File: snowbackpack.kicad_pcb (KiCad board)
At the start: 2 copper layers, 39.6 x 18 mm, 86 parts, among them J10 Conn_01x01_Pin, J11 Conn_01x01_Pin, J12 Conn_01x01_Pin, J13 Conn_01x01_Pin, J2 Conn_01x01_Pin, J3 Conn_01x01_Pin, J4 Conn_01x01_Pin, J5 Conn_01x01_Pin, J6 Conn_01x01_Pin, J7 Conn_01x01_Pin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

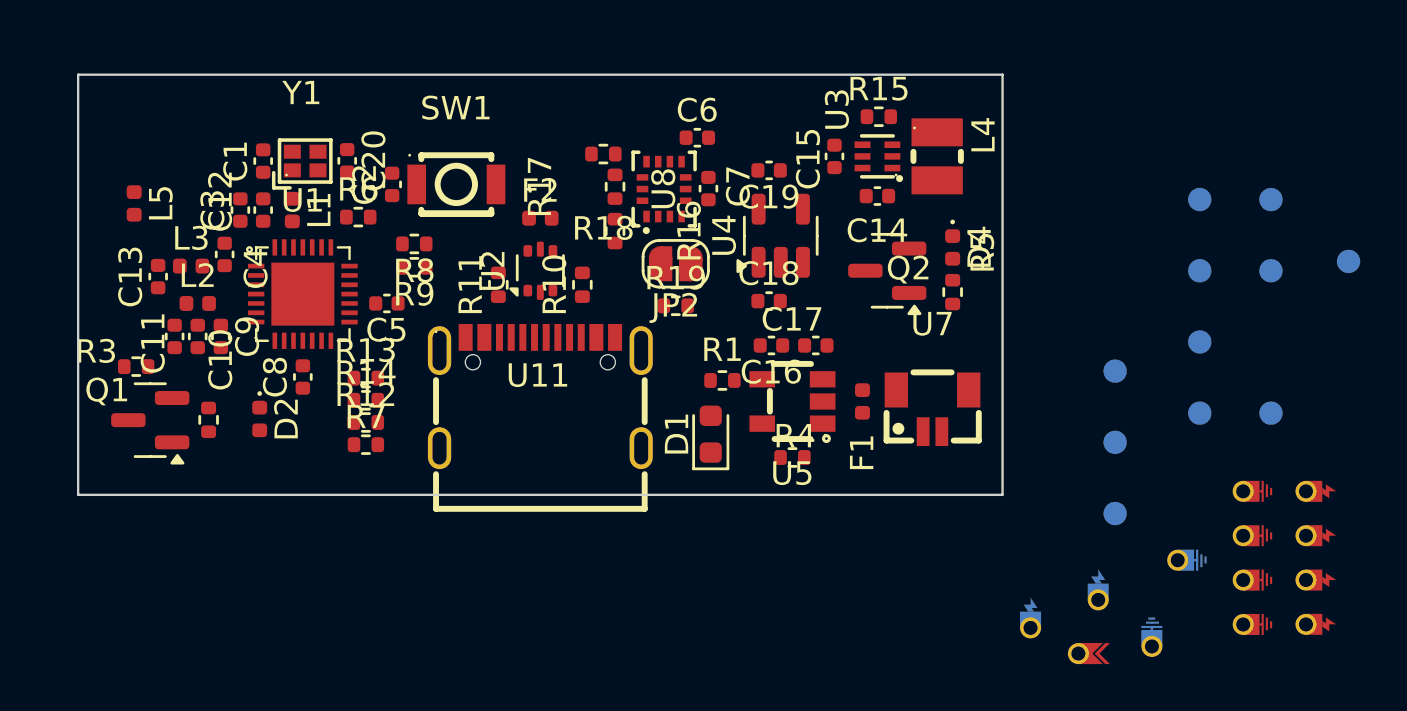
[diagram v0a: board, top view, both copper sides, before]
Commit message: First pcb routing
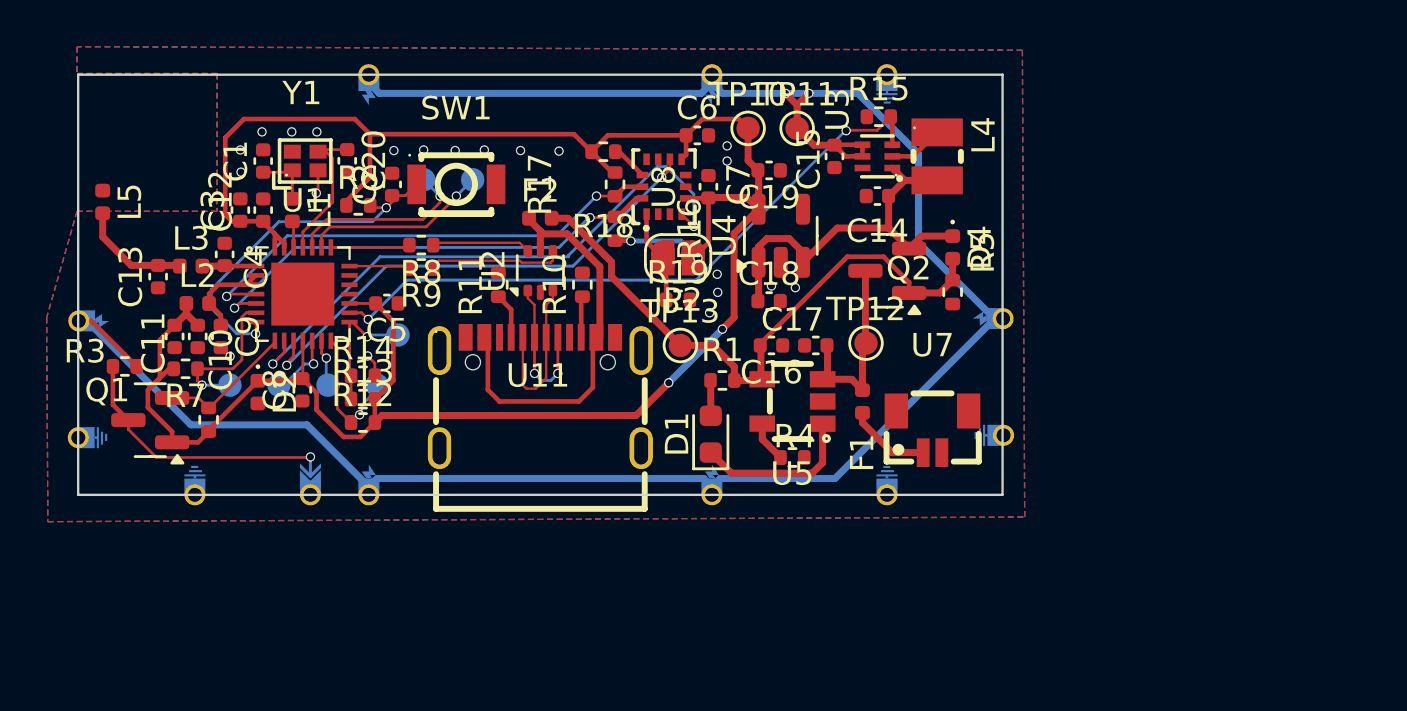
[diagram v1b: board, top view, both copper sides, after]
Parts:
- removed J12: Conn_01x01_Pin, Custom:matrix-pad-gn
- J10, J11, J13, J6, J7, J8, J9, JP1: moved to B.Cu
- TP10, TP11, TP12, TP13: moved to F.Cu
- moved J2 46.1 mm to (74.6, 97.5), turned to 0 degrees
- moved J8 45.8 mm to (86.5, 82.6), turned to -90 degrees
- moved J3 44.5 mm to (74.6, 92.5), turned to 0 degrees
- moved TP5 43.2 mm to (82.6, 95.3)
- moved J4 42.9 mm to (79.0, 99.4), turned to 90 degrees
- moved TP6 40.7 mm to (84.7, 95.3)
- moved TP14 37.9 mm to (80.5, 95.3)
- moved TP9 37.7 mm to (90.9, 86.5)
- moved TP8 37.7 mm to (88.8, 86.5)
- moved JP1 34.4 mm to (83.9, 99.4), turned to 90 degrees
- moved J7 32.3 mm to (101.2, 82.6), turned to -90 degrees
- moved TP15 31.7 mm to (86.8, 95.3)
- moved TP16 31.7 mm to (87.7, 93.2)
- moved J5 28.9 mm to (86.4, 99.4)
- moved J9 26.8 mm to (101.1, 99.4), turned to 90 degrees
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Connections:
- JP1 pad 1: Net-(JP1-A) -> unconnected-(JP1-A-Pad1)
- JP1 pad 2: unconnected-(JP1-B-Pad2) -> Net-(JP1-B)
- Q1 pad 3: Net-(JP1-A) -> Net-(JP1-B)
- R3 pad 2: Net-(JP1-A) -> Net-(JP1-B)
- U1 pad 4: SDA -> SCL
- U1 pad 5: SCL -> SDA
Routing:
- net VDD33: track 0.02 -> 103.3 mm, vias 0 -> 4
- net VDD5: track 0.00 -> 89.1 mm, vias 0 -> 2
- net 5VEN: track 0.00 -> 28.1 mm, vias 0 -> 2
- net VCCUSB: track 0.00 -> 26.0 mm
- net INT1: track 0.00 -> 25.4 mm, vias 0 -> 2
- net INT2: track 0.00 -> 21.5 mm, vias 0 -> 2
- net SCL: track 0.00 -> 21.1 mm, vias 0 -> 2
- net SDA: track 0.00 -> 20.4 mm, vias 0 -> 2
- net VCCUSBC: track 0.07 -> 17.5 mm
- net VIN: track 0.00 -> 17.1 mm
- net CHIP_EN: track 0.00 -> 15.3 mm, vias 0 -> 2
- net Net-(JP1-B): track 0.00 -> 12.0 mm, vias 0 -> 1
- net VBAT: track 0.00 -> 8.73 mm
- net Net-(U1-U0RXD): track 0.00 -> 7.99 mm, vias 0 -> 1
- net Net-(U1-U0TXD): track 0.00 -> 7.87 mm, vias 0 -> 1
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- added copper zone on B.Cu, net GND
- added copper zone on F.Cu, net GND

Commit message: Fixed smd antenna
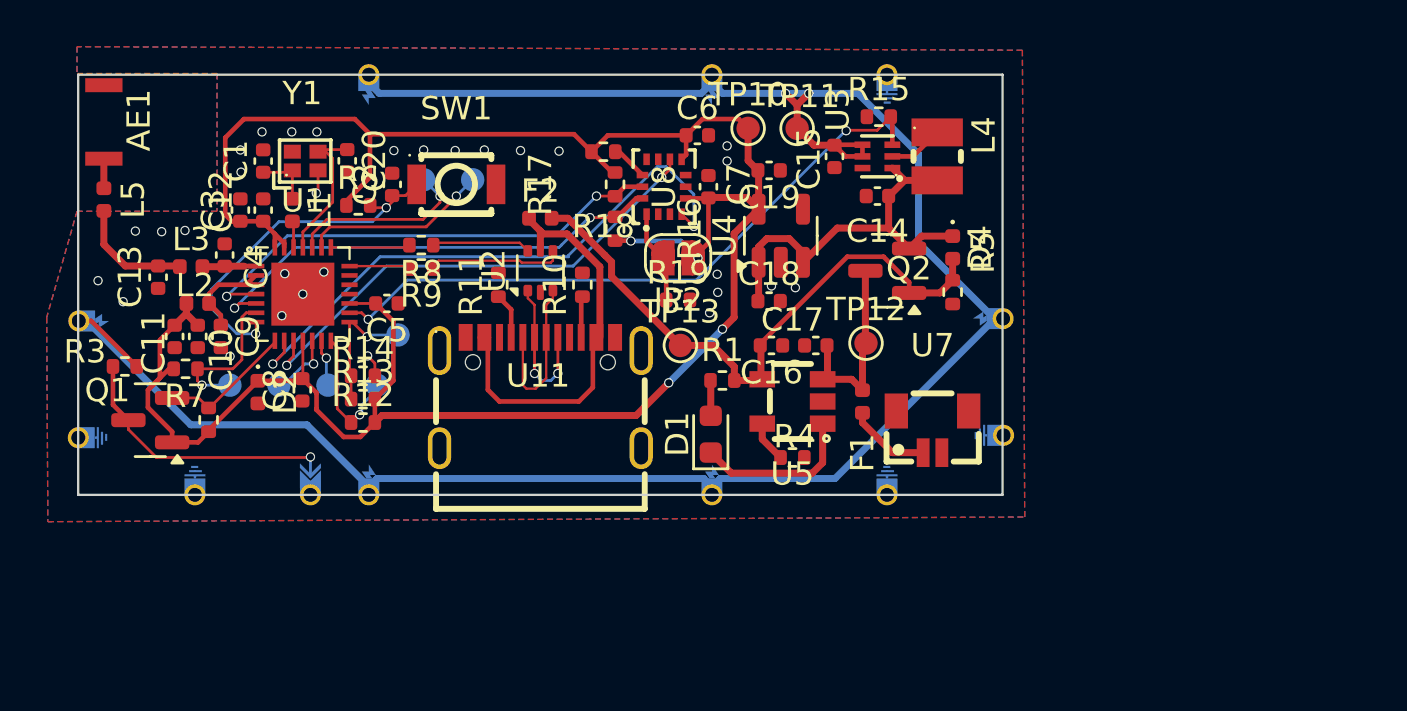
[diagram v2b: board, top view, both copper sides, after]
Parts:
- added AE1: Ceramic, Custom:CW324S, F.Cu at (75.1, 82.5)
- moved L5 0.11 mm to (75.1, 87.3)
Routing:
- net Net-(AE1-PCB_Trace): track 0.00 -> 1.27 mm
- net GND: vias 21 -> 30
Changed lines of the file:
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@@
 		(tenting front back)
 		(pcbplotparams
-			(layerselection 0x00000000_00000000_55555555_5755f5ff)
+			(layerselection 0x00000000_00000000_55555555_5755f55f)
 			(plot_on_all_layers_selection 0x00000000_00000000_00000000_00000000)
 			(disableapertmacros no)
-			(usegerberextensions no)
-			(usegerberattributes yes)
-			(usegerberadvancedattributes yes)
-			(creategerberjobfile yes)
+			(usegerberextensions yes)
+			(usegerberattributes no)
+			(usegerberadvancedattributes no)
+			(creategerberjobfile no)
 			(dashed_line_dash_ratio 12.000000)
 			(dashed_line_gap_ratio 3.000000)
@@
 			(sketchdnponfab yes)
 			(crossoutdnponfab yes)
-			(subtractmaskfromsilk no)
+			(subtractmaskfromsilk yes)
 			(outputformat 1)
 			(mirror no)
-			(drillshape 1)
+			(drillshape 0)
 			(scaleselection 1)
-			(outputdirectory "")
+			(outputdirectory "test1")
 		)
 	)
@@
 	(net 53 "unconnected-(JP1-A-Pad1)")
 	(net 54 "unconnected-(JP1-A-Pad1)_1")
+	(net 55 "unconnected-(AE1-FEED-Pad1)")
 	(footprint "Resistor_SMD:R_0402_1005Metric"
 		(layer "F.Cu")
@@
 	(footprint "Inductor_SMD:L_0402_1005Metric"
 		(layer "F.Cu")
-		(at 75.05 87.45 -90)
+		(at 75.1 87.35 -90)
 		(descr "Inductor SMD 0402 (1005 Metric), square (rectangular) end terminal, IPC_7351 nominal, (Body size source: http://www.tortai-tech.com/upload/download/2011102023233369053.pdf), generated with kicad-footprint-generator")
 		(tags "inductor")
 		(property "Reference" "L5"
-			(at 0 -1.17 90)
+			(at 0 -1.25 90)
 			(layer "F.SilkS")
 			(effects
@@
 	(footprint "Capacitor_SMD:C_0402_1005Metric"
 		(layer "F.Cu")
-		(at 80.274994 89.7 -90)
+		(at 80.274994 89.725 -90)
 		(descr "Capacitor SMD 0402 (1005 Metric), square (rectangular) end terminal, IPC_7351 nominal, (Body size source: IPC-SM-782 page 76, https://www.pcb-3d.com/wordpress/wp-content/uploads/ipc-sm-782a_amendment_1_and_2.pdf), generated with kicad-footprint-generator")
 		(tags "capacitor")
@@
 	(footprint "Inductor_SMD:L_0402_1005Metric"
 		(layer "F.Cu")
-		(at 78.838724 90.2)
+		(at 78.838724 90.225)
 		(descr "Inductor SMD 0402 (1005 Metric), square (rectangular) end terminal, IPC_7351 nominal, (Body size source: http://www.tortai-tech.com/upload/download/2011102023233369053.pdf), generated with kicad-footprint-generator")
 		(tags "inductor")
@@
 		)
 	)
+	(footprint "Custom:CW324S"
+		(layer "F.Cu")
+		(at 75.1 82.45 -90)
+		(property "Reference" "AE1"
+			(at 1.5 -1.5 90)
+			(unlocked yes)
+			(layer "F.SilkS")
+			(effects
+				(font
+					(size 1 1)
+					(thickness 0.1)
+				)
+			)
+		)
+		(property "Value" "Ceramic"
+			(at -1.5 -8 270)
+			(unlocked yes)
+			(layer "F.Fab")
+			(effects
+				(font
+					(size 1 1)
+					(thickness 0.15)
+				)
+			)
+		)
+		(property "Datasheet" ""
+			(at -1.5 -9 270)
+			(unlocked yes)
+			(layer "F.Fab")
+			(hide yes)
+			(effects
+				(font
+					(size 1 1)
+					(thickness 0.15)
+				)
+			)
+		)
+		(property "Description" "Ceramic chip antenna with pin for PCB trace"
+			(at -1.5 -9 270)
+			(unlocked yes)
+			(layer "F.Fab")
+			(hide yes)
+			(effects
+				(font
+					(size 1 1)
+					(thickness 0.15)
+				)
+			)
+		)
+		(sheetname "/")
+		(sheetfile "snowbackpack.kicad_sch")
+		(attr smd)
+		(fp_text user "${REFERENCE}"
+			(at -1 -6.5 270)
+			(unlocked yes)
+			(layer "F.Fab")
+			(effects
+				(font
+					(size 1 1)
+					(thickness 0.15)
+				)
+			)
+		)
+		(pad "1" smd rect
+			(at 0 0 270)
+			(size 0.6 1.6)
+			(layers "F.Cu" "F.Mask" "F.Paste")
+			(net 55 "unconnected-(AE1-FEED-Pad1)")
+			(pinfunction "FEED")
+			(pintype "input+no_connect")
+			(thermal_bridge_angle 45)
+		)
+		(pad "2" smd rect
+			(at 3.149999 0 270)
+			(size 0.6 1.6)
+			(layers "F.Cu" "F.Mask" "F.Paste")
+			(net 7 "Net-(AE1-PCB_Trace)")
+			(pinfunction "PCB_Trace")
+			(pintype "passive")
+			(thermal_bridge_angle 45)
+		)
+		(embedded_fonts no)
+	)
 	(footprint "Resistor_SMD:R_0402_1005Metric"
 		(layer "F.Cu")
@@
 		(tags "inductor")
 		(property "Reference" "L2"
-			(at 0 -1.17 0)
+			(at -0.121567 -0.775 0)
 			(layer "F.SilkS")
 			(effects
@@
 		(tags "test point SMD pad")
 		(property "Reference" "TP11"
-			(at 0 -1.448 0)
+			(at 0.125 -1.375 0)
 			(layer "F.SilkS")
 			(effects
@@
 	(footprint "Capacitor_SMD:C_0402_1005Metric"
 		(layer "F.Cu")
-		(at 77.424509 90.65 90)
+		(at 77.424509 90.675 90)
 		(descr "Capacitor SMD 0402 (1005 Metric), square (rectangular) end terminal, IPC_7351 nominal, (Body size source: IPC-SM-782 page 76, https://www.pcb-3d.com/wordpress/wp-content/uploads/ipc-sm-782a_amendment_1_and_2.pdf), generated with kicad-footprint-generator")
 		(tags "capacitor")
 		(property "Reference" "C13"
-			(at 0 -1.16 90)
+			(at 0.025 -1.199509 90)
 			(layer "F.SilkS")
 			(effects
@@
 	)
 	(segment
+		(start 75.1 86.865)
+		(end 75.1 85.599999)
+		(width 0.3)
+		(layer "F.Cu")
+		(net 7)
+	)
+	(segment
 		(start 87.5 87.23)
 		(end 87.45 87.18)
@@
 	)
 	(via
+		(at 82.725 92.325)
+		(size 0.4)
+		(drill 0.3)
+		(layers "F.Cu" "B.Cu")
+		(net 19)
+	)
+	(via
 		(at 80.50473 94.06973)
 		(size 0.4)
@@
 	)
 	(via
+		(at 75.925 91.725)
+		(size 0.4)
+		(drill 0.3)
+		(layers "F.Cu" "B.Cu")
+		(free yes)
+		(net 19)
+	)
+	(via
 		(at 90.15 85.25)
 		(size 0.4)
@@
 	)
 	(via
+		(at 84.525 90.45)
+		(size 0.4)
+		(drill 0.3)
+		(layers "F.Cu" "B.Cu")
+		(net 19)
+	)
+	(via
+		(at 82.85 90.525)
+		(size 0.4)
+		(drill 0.3)
+		(layers "F.Cu" "B.Cu")
+		(net 19)
+	)
+	(via
+		(at 76.45 88.7)
+		(size 0.4)
+		(drill 0.3)
+		(layers "F.Cu" "B.Cu")
+		(free yes)
+		(net 19)
+	)
+	(via
 		(at 92.95 85.25)
 		(size 0.4)
@@
 	)
 	(via
+		(at 77.575 88.725)
+		(size 0.4)
+		(drill 0.3)
+		(layers "F.Cu" "B.Cu")
+		(free yes)
+		(net 19)
+	)
+	(via
 		(at 88.8 85.225)
 		(size 0.4)
@@
 	)
 	(via
+		(at 83.624994 91.400255)
+		(size 0.4)
+		(drill 0.3)
+		(layers "F.Cu" "B.Cu")
+		(net 19)
+	)
+	(via
 		(at 101.375 90.55)
 		(size 0.4)
@@
 	)
 	(via
+		(at 74.85 90.825)
+		(size 0.4)
+		(drill 0.3)
+		(layers "F.Cu" "B.Cu")
+		(free yes)
+		(net 19)
+	)
+	(via
 		(at 84.225 84.45)
 		(size 0.4)
@@
 	)
 	(via
+		(at 78.575 88.675)
+		(size 0.4)
+		(drill 0.3)
+		(layers "F.Cu" "B.Cu")
+		(free yes)
+		(net 19)
+	)
+	(via
 		(at 94.6 85.275)
 		(size 0.4)
@@
 	)
 	(segment
-		(start 80.498898 90.198898)
-		(end 81.624993 90.198898)
-		(width 0.2)
-		(layer "F.Cu")
-		(net 22)
-	)
-	(segment
 		(start 80.295096 90.200102)
 		(end 80.274994 90.18)
@@
 	)
 	(segment
-		(start 79.323724 90.2)
-		(end 80.254994 90.2)
+		(start 79.323724 90.225)
+		(end 80.254994 90.225)
 		(width 0.3)
 		(layer "F.Cu")
@@
 	)
 	(segment
-		(start 80.48 90.18)
-		(end 80.498898 90.198898)
+		(start 81.148898 90.198898)
+		(end 81.624993 90.198898)
 		(width 0.2)
 		(layer "F.Cu")
@@
 	)
 	(segment
+		(start 80.274994 90.205)
+		(end 81.12 90.205)
+		(width 0.3)
+		(layer "F.Cu")
+		(net 22)
+	)
+	(segment
 		(start 106.42 85)
 		(end 106.4 85.02)
@@
 	)
 	(segment
-		(start 77.424509 90.17)
-		(end 76.27 90.17)
+		(start 77.424509 90.195)
+		(end 78.323724 90.195)
 		(width 0.3)
 		(layer "F.Cu")
@@
 	)
 	(segment
-		(start 77.424509 90.17)
-		(end 78.323724 90.17)
+		(start 78.323724 90.195)
+		(end 78.353724 90.225)
 		(width 0.3)
 		(layer "F.Cu")
@@
 	)
 	(segment
-		(start 78.323724 90.17)
-		(end 78.353724 90.2)
+		(start 76.02 90.195)
+		(end 77.424509 90.195)
 		(width 0.3)
 		(layer "F.Cu")
@@
 	)
 	(segment
-		(start 77.454509 90.2)
-		(end 77.424509 90.17)
+		(start 77.454509 90.225)
+		(end 77.424509 90.195)
 		(width 0.1)
 		(layer "F.Cu")
@@
 	)
 	(segment
-		(start 76.27 90.17)
-		(end 75.05 88.95)
+		(start 75.1 89.275)
+		(end 76.02 90.195)
 		(width 0.3)
 		(layer "F.Cu")
@@
 	)
 	(segment
-		(start 75.05 88.95)
-		(end 75.05 87.935)
+		(start 75.1 87.86)
+		(end 75.1 89.275)
 		(width 0.3)
 		(layer "F.Cu")

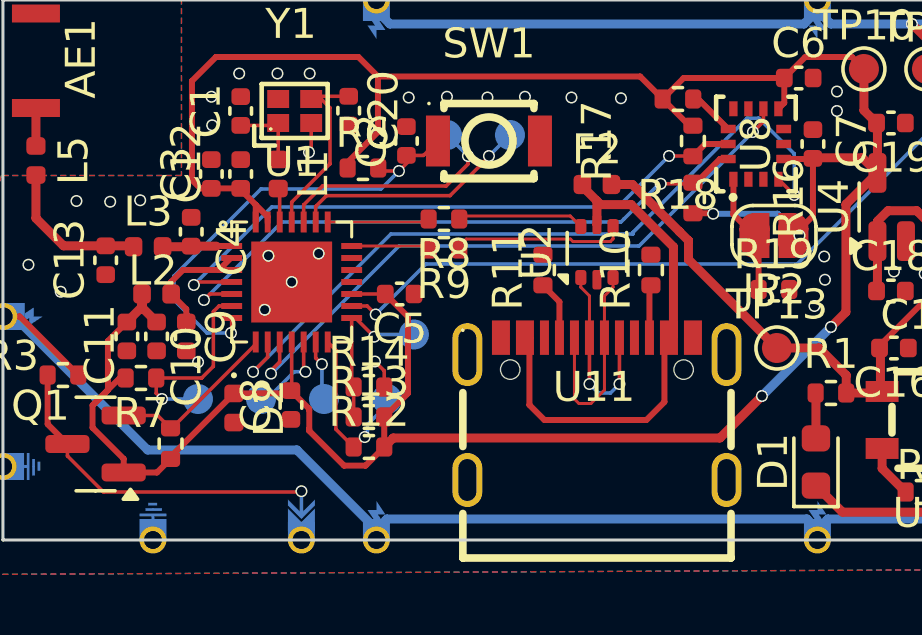
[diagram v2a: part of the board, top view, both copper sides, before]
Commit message: Routed USB
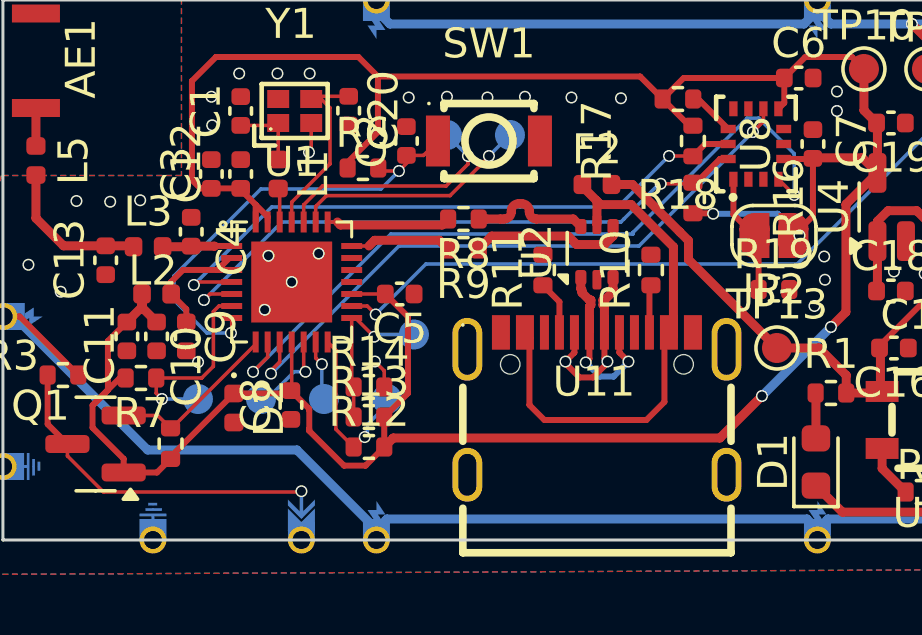
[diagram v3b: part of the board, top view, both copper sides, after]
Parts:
- moved R8 0.65 mm to (89.3, 89.3)
- moved R9 0.65 mm to (89.3, 90.3)
- moved U11 0.18 mm to (93.8, 95.5)
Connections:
- net USBCD+ renamed /USBCD+
- net USBCD- renamed /USBCD-
- net USBD+ renamed /USBD+
- net USBD- renamed /USBD-
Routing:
- net /USBCD-: track 7.16 -> 6.03 mm, vias 0 -> 2
- net Net-(U1-GPIO18): track 2.57 -> 3.66 mm
- net Net-(U1-GPIO19): track 3.45 -> 4.46 mm
